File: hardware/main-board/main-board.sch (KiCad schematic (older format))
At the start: 31 parts

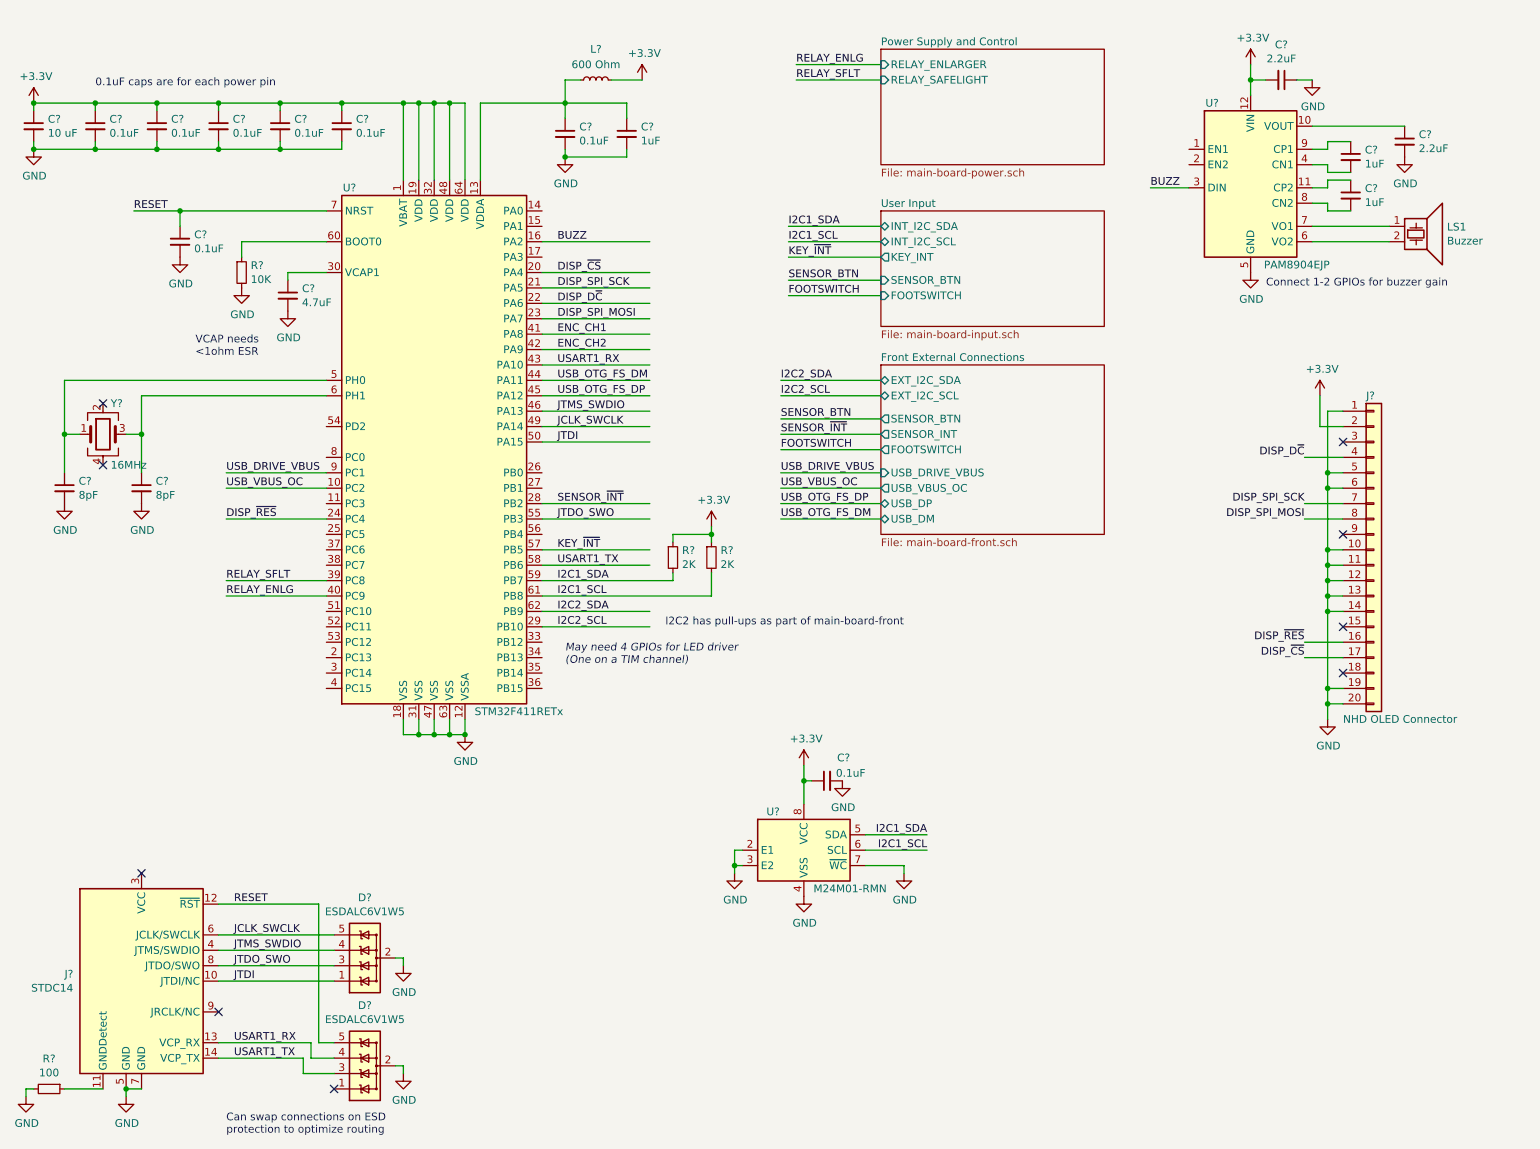
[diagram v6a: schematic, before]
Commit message: Added LED driver to schematics
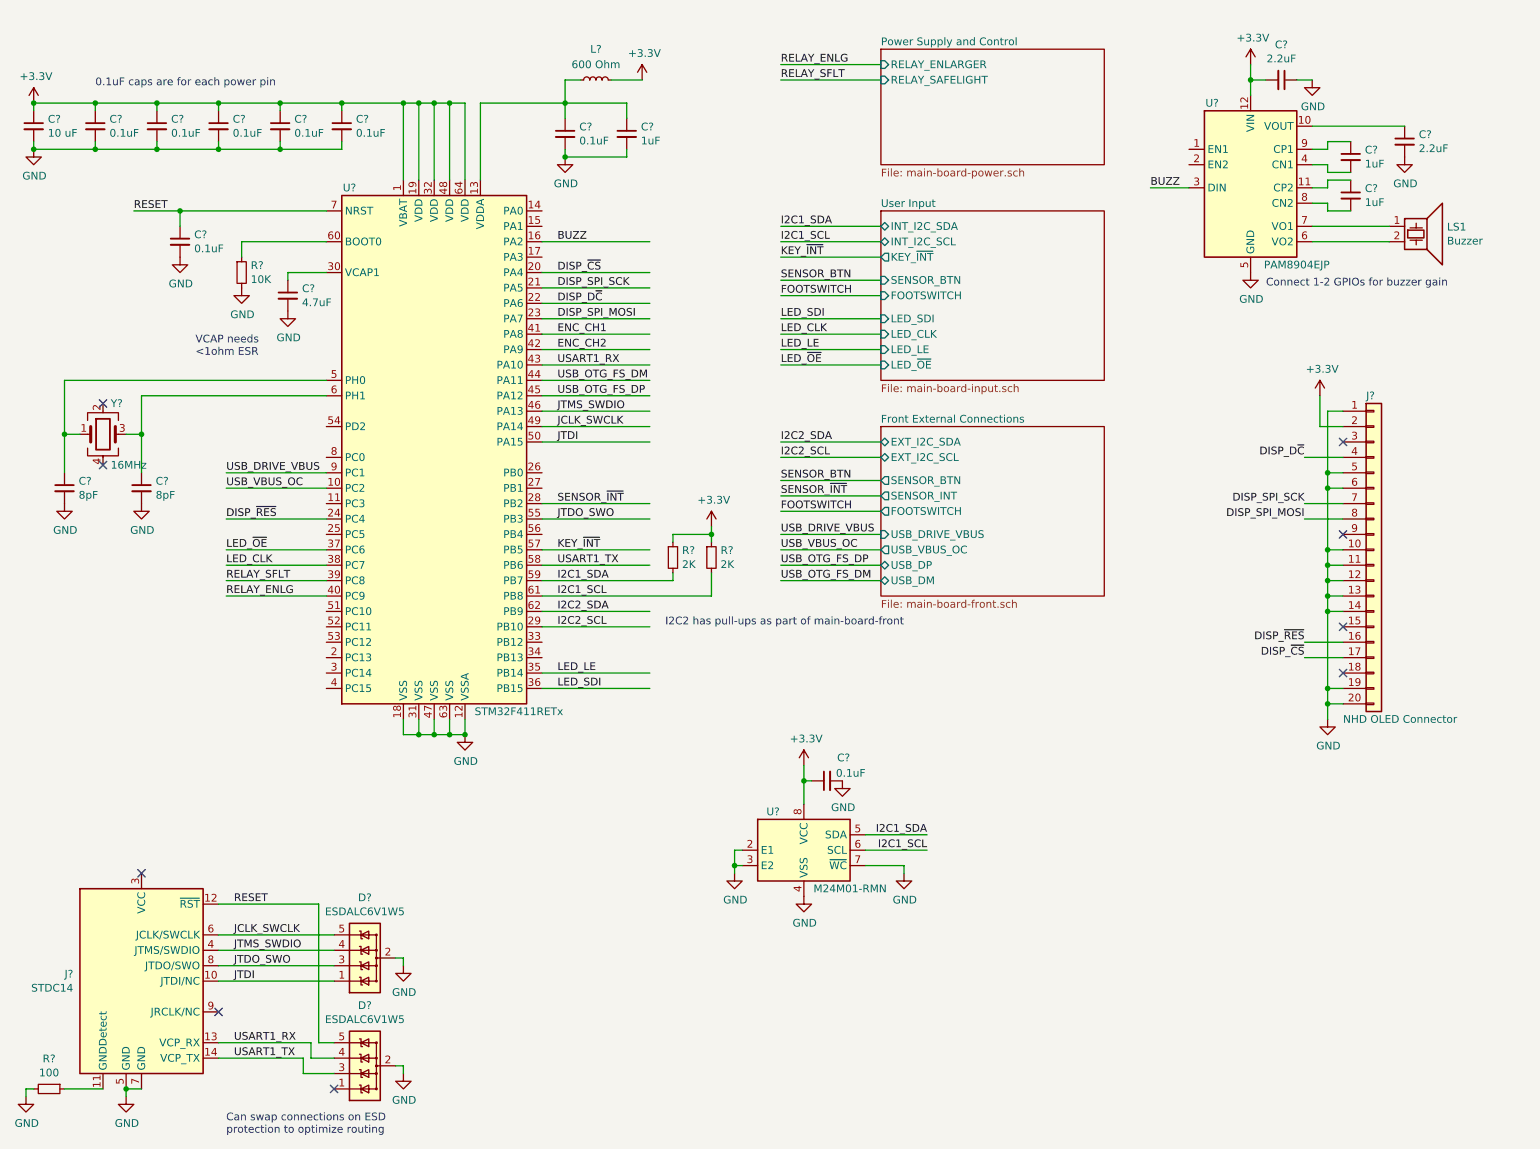
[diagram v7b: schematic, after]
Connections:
- net labels added: LED_CLK, LED_LE, LED_SDI, LED_~OE
- wire segments 195 -> 203
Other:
- note removed: "May need 4 GPIOs for LED driver\n(One on a TIM channel)"
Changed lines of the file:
@@
 $EndSheet
 $Sheet
-S 6500 1750 1450 750
+S 6500 1750 1450 1100
 U 5F8B69B5
 F0 "User Input" 50
@@
 F4 "SENSOR_BTN" I L 6500 2200 50
 F5 "FOOTSWITCH" I L 6500 2300 50
-F6 "KEY_INT" O L 6500 2050 50
+F6 "LED_SDI" I L 6500 2450 50
+F7 "LED_CLK" I L 6500 2550 50
+F8 "LED_LE" I L 6500 2650 50
+F9 "LED_~OE" I L 6500 2750 50
+F10 "KEY_~INT" O L 6500 2050 50
 $EndSheet
 $Comp
@@
 DISP_~CS
 $Sheet
-S 6500 2750 1450 1100
+S 6500 3150 1450 1100
 U 5FA19AFF
 F0 "Front External Connections" 50
 F1 "main-board-front.sch" 50
-F2 "EXT_I2C_SDA" B L 6500 2850 50
-F3 "EXT_I2C_SCL" B L 6500 2950 50
-F4 "SENSOR_BTN" O L 6500 3100 50
-F5 "SENSOR_INT" O L 6500 3200 50
-F6 "FOOTSWITCH" O L 6500 3300 50
-F7 "USB_DRIVE_VBUS" I L 6500 3450 50
-F8 "USB_VBUS_OC" O L 6500 3550 50
-F9 "USB_DP" B L 6500 3650 50
-F10 "USB_DM" B L 6500 3750 50
+F2 "EXT_I2C_SDA" B L 6500 3250 50
+F3 "EXT_I2C_SCL" B L 6500 3350 50
+F4 "SENSOR_BTN" O L 6500 3500 50
+F5 "SENSOR_INT" O L 6500 3600 50
+F6 "FOOTSWITCH" O L 6500 3700 50
+F7 "USB_DRIVE_VBUS" I L 6500 3850 50
+F8 "USB_VBUS_OC" O L 6500 3950 50
+F9 "USB_DP" B L 6500 4050 50
+F10 "USB_DM" B L 6500 4150 50
 $EndSheet
 $Comp
@@
 Wire Wire Line
 	4300 3950 5000 3950
-Text Notes 4450 4700 0    50   Italic 0
-May need 4 GPIOs for LED driver\n(One on a TIM channel)
 Wire Wire Line
 	2200 6250 2850 6250
@@
 Can swap connections on ESD\nprotection to optimize routing
 NoConn ~ 1700 6050
-Text Label 5850 2950 0    50   ~ 0
+Text Label 5850 3350 0    50   ~ 0
 I2C2_SCL
-Text Label 5850 2850 0    50   ~ 0
+Text Label 5850 3250 0    50   ~ 0
 I2C2_SDA
-Text Label 5850 3200 0    50   ~ 0
+Text Label 5850 3600 0    50   ~ 0
 SENSOR_~INT
-Text Label 5850 3750 0    50   ~ 0
+Text Label 5850 4150 0    50   ~ 0
 USB_OTG_FS_DM
-Text Label 5850 3650 0    50   ~ 0
+Text Label 5850 4050 0    50   ~ 0
 USB_OTG_FS_DP
-Text Label 5850 3450 0    50   ~ 0
+Text Label 5850 3850 0    50   ~ 0
 USB_DRIVE_VBUS
-Text Label 5850 3550 0    50   ~ 0
+Text Label 5850 3950 0    50   ~ 0
 USB_VBUS_OC
 Wire Wire Line
-	6500 2850 5850 2850
-Wire Wire Line
-	5850 2950 6500 2950
-Wire Wire Line
-	5850 3200 6500 3200
-Wire Wire Line
-	6500 3450 5850 3450
-Wire Wire Line
-	5850 3550 6500 3550
-Wire Wire Line
-	5850 3650 6500 3650
-Wire Wire Line
-	5850 3750 6500 3750
-Text Label 5900 2200 0    50   ~ 0
+	6500 3250 5850 3250
+Wire Wire Line
+	5850 3350 6500 3350
+Wire Wire Line
+	5850 3600 6500 3600
+Wire Wire Line
+	6500 3850 5850 3850
+Wire Wire Line
+	5850 3950 6500 3950
+Wire Wire Line
+	5850 4050 6500 4050
+Wire Wire Line
+	5850 4150 6500 4150
+Text Label 5850 2200 0    50   ~ 0
 SENSOR_BTN
-Text Label 5900 2300 0    50   ~ 0
+Text Label 5850 2300 0    50   ~ 0
 FOOTSWITCH
-Text Label 5850 3100 0    50   ~ 0
+Text Label 5850 3500 0    50   ~ 0
 SENSOR_BTN
-Text Label 5850 3300 0    50   ~ 0
+Text Label 5850 3700 0    50   ~ 0
 FOOTSWITCH
 Wire Wire Line
-	6500 2200 5900 2200
-Wire Wire Line
-	5900 2300 6500 2300
-Wire Wire Line
-	5850 3300 6500 3300
-Wire Wire Line
-	5850 3100 6500 3100
-Text Label 5900 1850 0    50   ~ 0
+	6500 2200 5850 2200
+Wire Wire Line
+	5850 2300 6500 2300
+Wire Wire Line
+	5850 3700 6500 3700
+Wire Wire Line
+	5850 3500 6500 3500
+Text Label 5850 1850 0    50   ~ 0
 I2C1_SDA
-Text Label 5900 1950 0    50   ~ 0
+Text Label 5850 1950 0    50   ~ 0
 I2C1_SCL
 Wire Wire Line
-	5900 1950 6500 1950
-Wire Wire Line
-	5900 1850 6500 1850
-Text Label 5900 2050 0    50   ~ 0
+	5850 1950 6500 1950
+Wire Wire Line
+	5850 1850 6500 1850
+Text Label 5850 2050 0    50   ~ 0
 KEY_~INT
 Wire Wire Line
-	5900 2050 6500 2050
+	5850 2050 6500 2050
 Text Notes 5100 4450 0    50   ~ 0
 I2C2 has pull-ups as part of main-board-front
-Text Label 5950 900  0    50   ~ 0
+Text Label 5850 900  0    50   ~ 0
 RELAY_SFLT
-Text Label 5950 800  0    50   ~ 0
+Text Label 5850 800  0    50   ~ 0
 RELAY_ENLG
 Wire Wire Line
-	6500 800  5950 800
-Wire Wire Line
-	6500 900  5950 900
+	6500 800  5850 800
+Wire Wire Line
+	6500 900  5850 900
 Text Label 2250 4150 0    50   ~ 0
 RELAY_SFLT
@@
 Text Notes 9000 2250 0    50   ~ 0
 Connect 1-2 GPIOs for buzzer gain
+Text Label 2250 4050 0    50   ~ 0
+LED_CLK
+Text Label 2250 3950 0    50   ~ 0
+LED_~OE
+Text Label 4400 4850 0    50   ~ 0
+LED_SDI
+Text Label 4400 4750 0    50   ~ 0
+LED_LE
+Wire Wire Line
+	2250 4050 2900 4050
+Wire Wire Line
+	2250 3950 2900 3950
+Wire Wire Line
+	4300 4750 5000 4750
+Wire Wire Line
+	4300 4850 5000 4850
+Text Label 5850 2750 0    50   ~ 0
+LED_~OE
+Text Label 5850 2550 0    50   ~ 0
+LED_CLK
+Text Label 5850 2650 0    50   ~ 0
+LED_LE
+Text Label 5850 2450 0    50   ~ 0
+LED_SDI
+Wire Wire Line
+	6500 2450 5850 2450
+Wire Wire Line
+	6500 2550 5850 2550
+Wire Wire Line
+	6500 2650 5850 2650
+Wire Wire Line
+	6500 2750 5850 2750
 $EndSCHEMATC

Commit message: Annotated schematic got ERC to pass
Annotated a few components manually, then let KiCad to the rest
automatically.

Added no-connection flags to all intentionally-unused pins.
Added comments next to no-connection pins that are likely to become used
soon.
Fixed USB power switch schematic symbol's output pin type.
Fixed IEC output jack schematic symbol pin types.
Rearranged power flags as needed to get ERC to pass.

In cases where power needs to flow through another component (switch,
fuse, inductor, etc) a power flag is needed to make ERC happy.

The Vcap pin on the STM32 schematic symbol seems to be designated as a
power input, even though this pin is only supposed to connect to a
capacitor to ground. Added a power flag to make ERC happy here, to avoid
duplicating a library symbol.
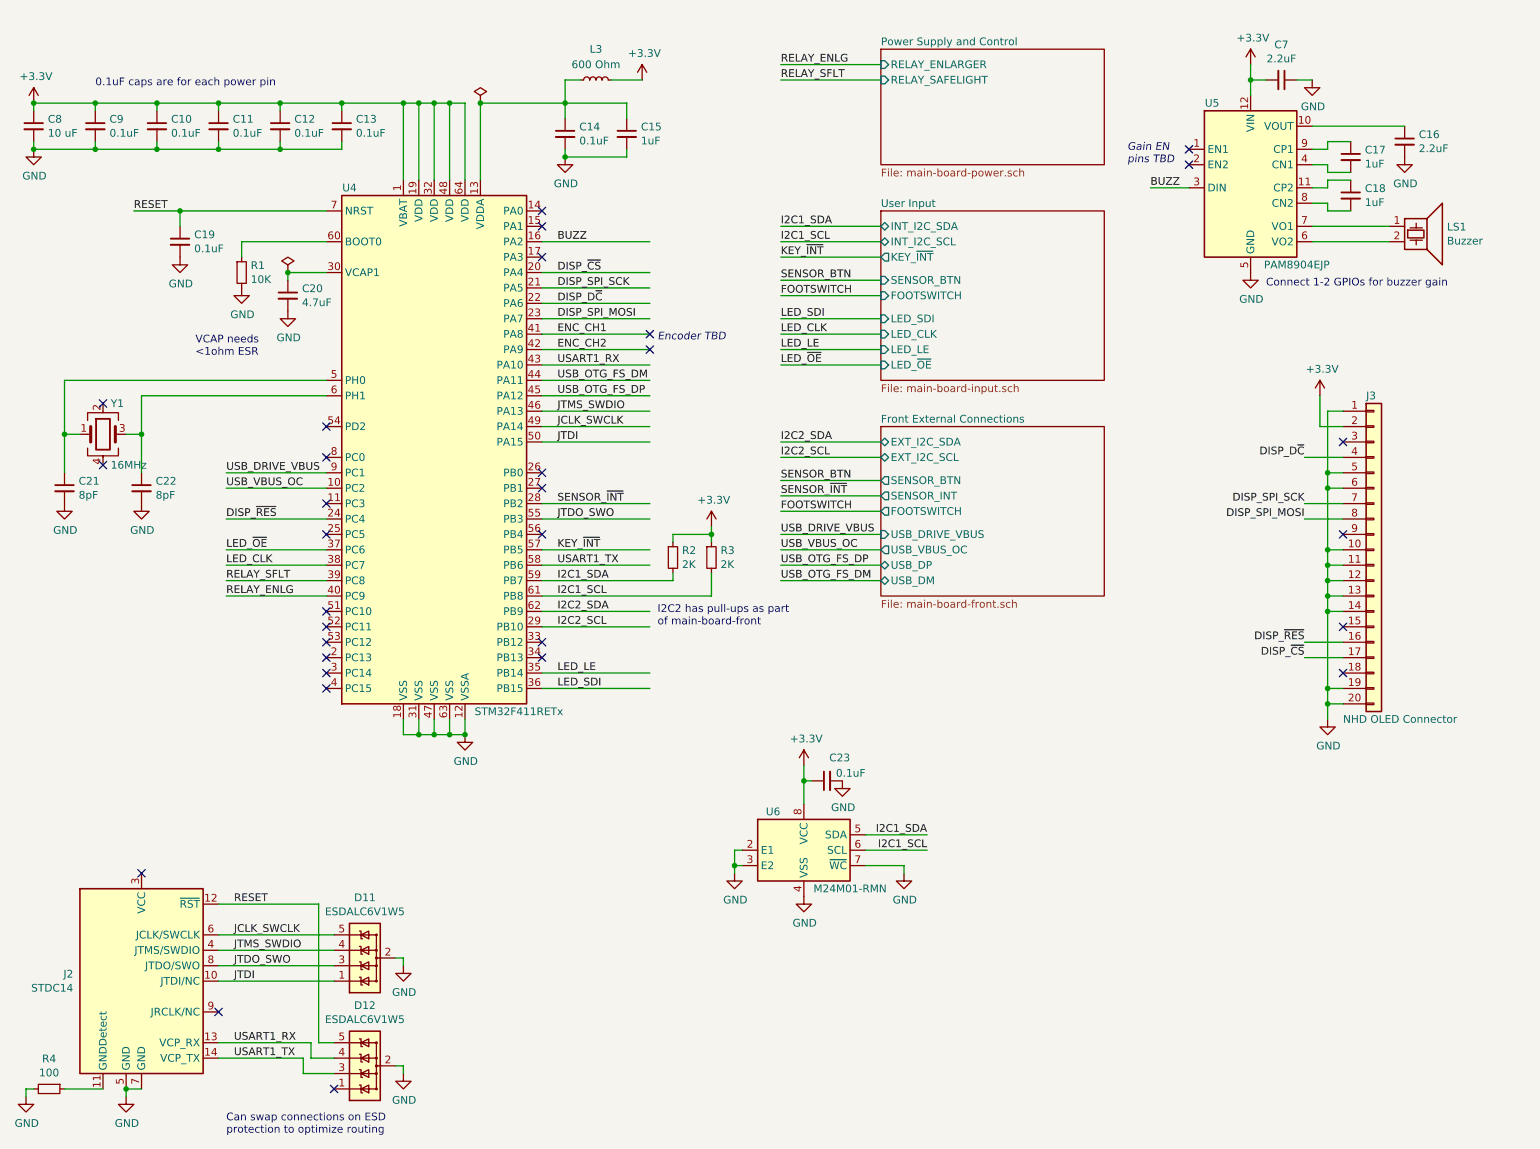
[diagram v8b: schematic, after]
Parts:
- J3: renamed from J?; footprint Connector_PinHeader_2.54mm:PinHeader_1x20_P2.54mm_Vertical -> Connector_PinSocket_2.54mm:PinSocket_1x20_P2.54mm_Vertical
- gave numbers to parts that had none: 29
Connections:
- no-connect marks 9 -> 31
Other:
- note added: "Encoder TBD"
- note added: "Gain EN\npins TBD"
- note added: "I2C2 has pull-ups as part\nof main-board-front"
- note removed: "I2C2 has pull-ups as part of main-board-front"
